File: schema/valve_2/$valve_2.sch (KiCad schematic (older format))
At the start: 114 parts, among them J1 DB37, J2 DB37, J3 DB9, P1 SETUP, P2 CROSS-BRD-1, P3 CROSS-BRD-2, P4 SWD-IAP, U1 74HC165, U10 L293, U11 L293, U12 L293, U13 L293, U14 MINI-USB-B, U2 74HC165, U3 74HC164, U4 74HC164, U5 74HC164, U6 74HC164, U7 L293, U8 L293, U9 L293, X1 8MHz

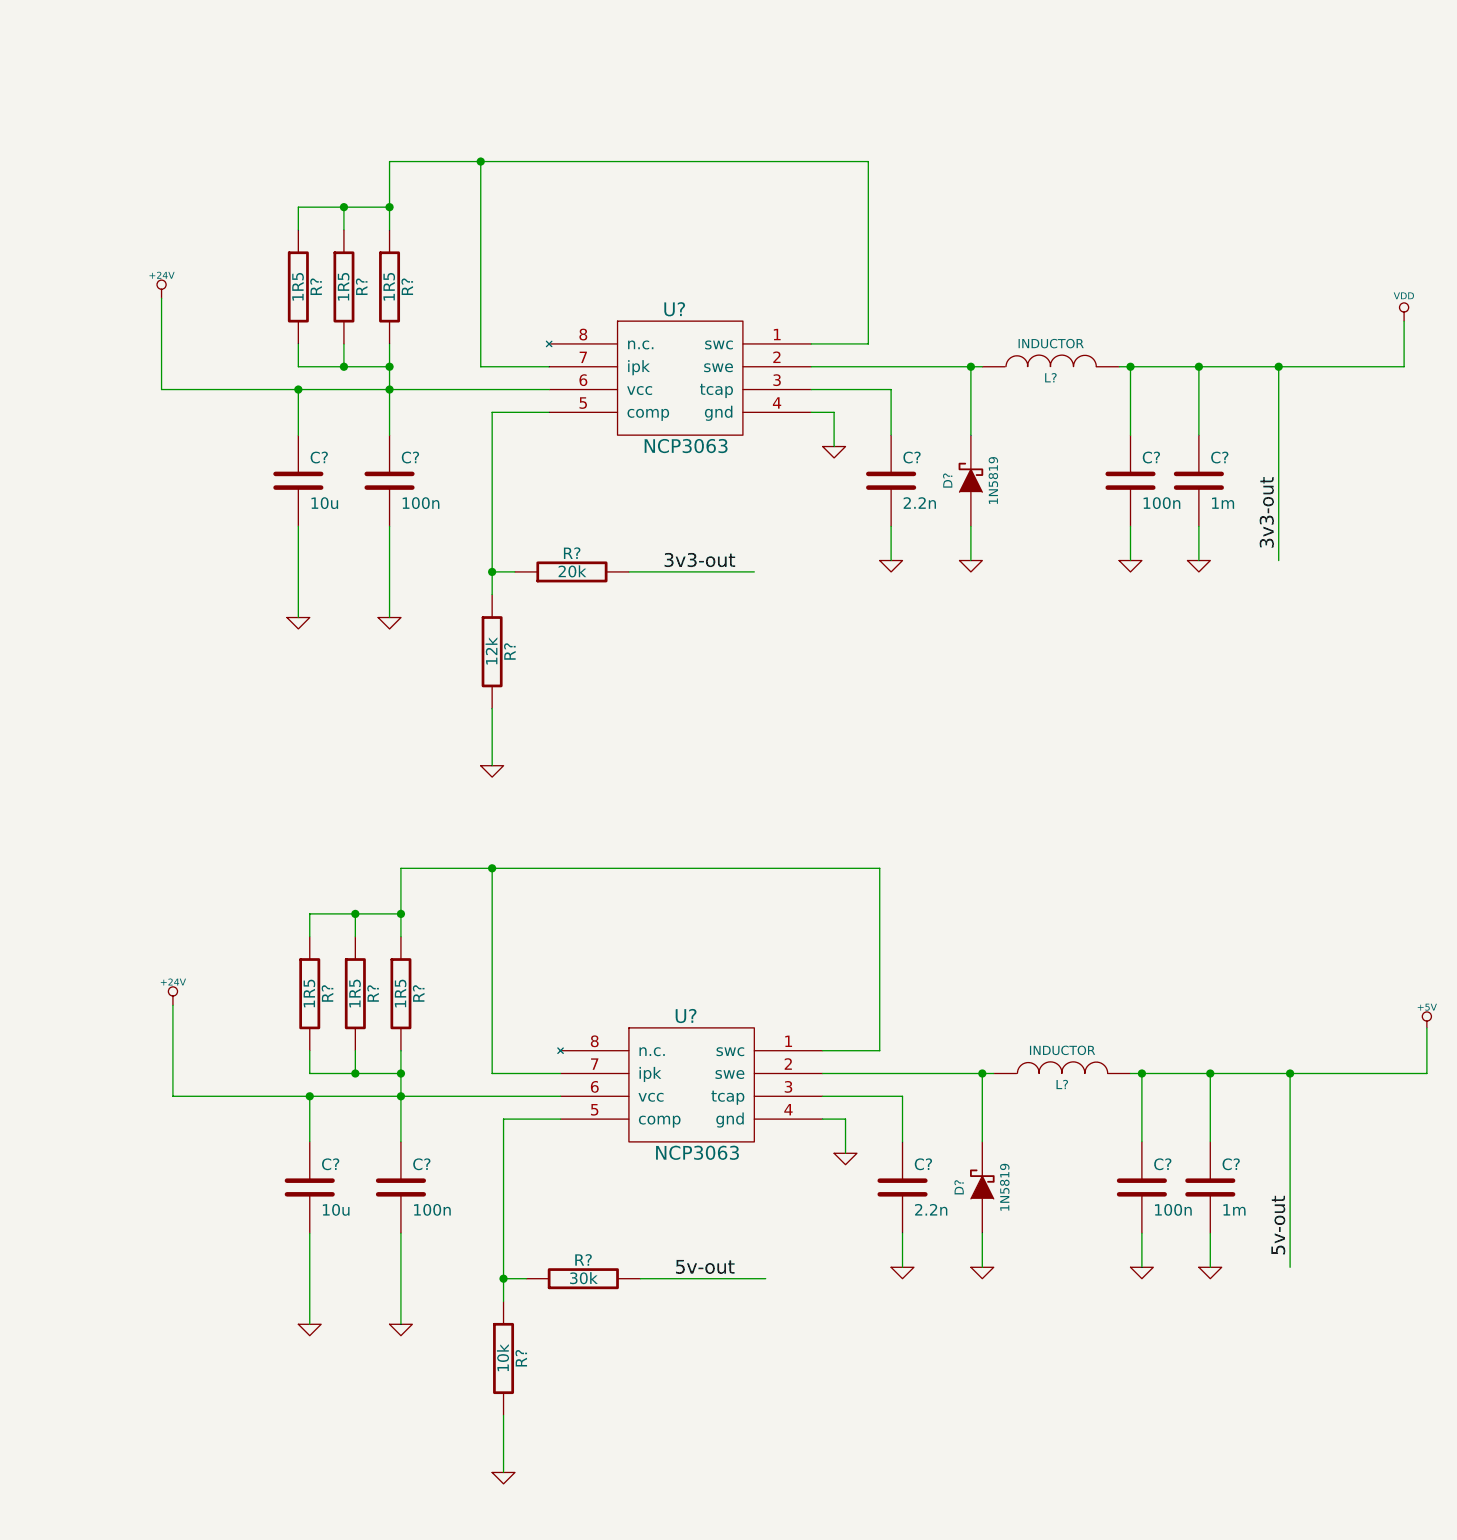
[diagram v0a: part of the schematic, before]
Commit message: Placing elements.
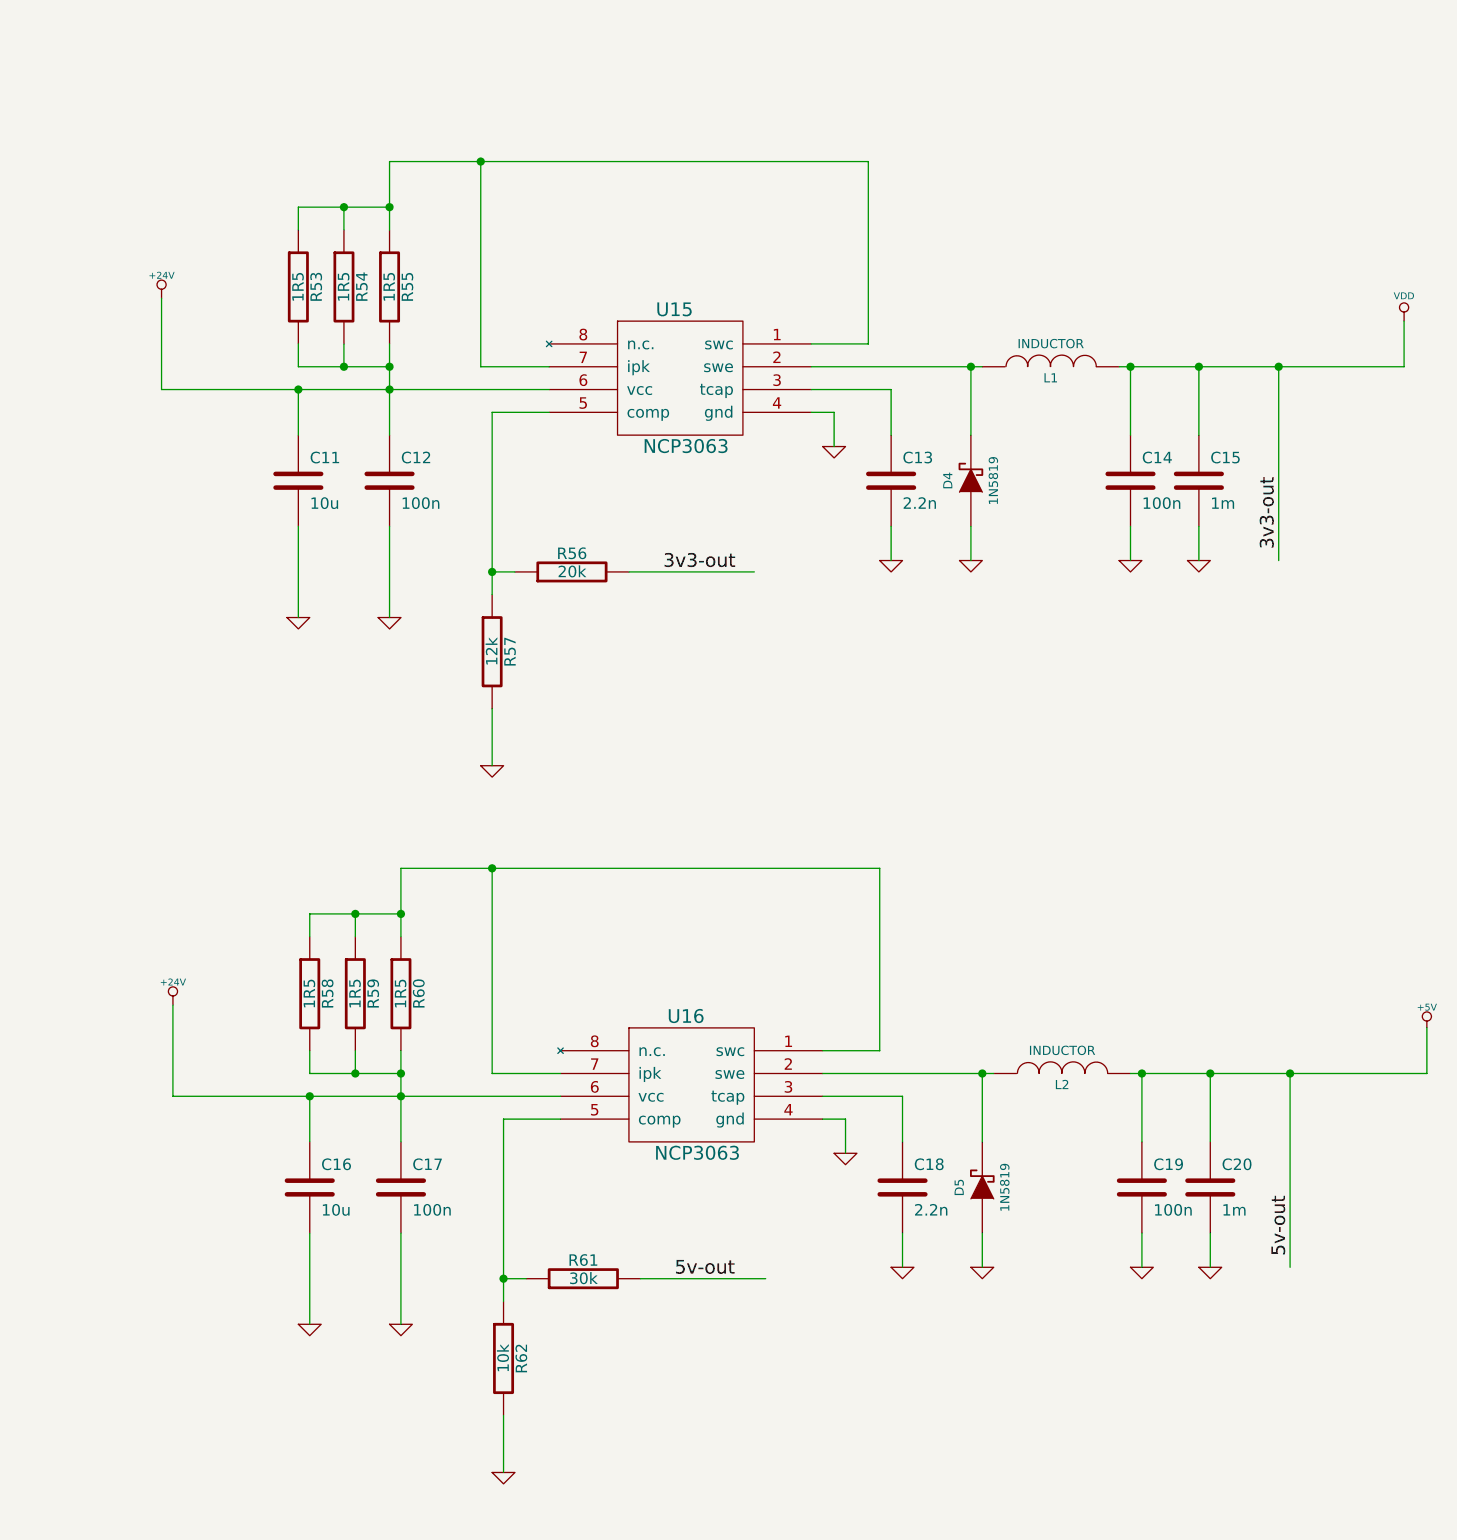
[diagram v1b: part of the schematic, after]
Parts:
- gave numbers to parts that had none: 26
